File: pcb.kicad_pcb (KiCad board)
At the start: 2 copper layers, 47 x 68 mm, 52 parts, among them J1 SWD, J10 Conn_02x04_Counter_Clockwise, J2 PWR, J3 MPU6050, J4 ENC1, J5 ENC2, J6 ENC3, J7 USB_C_Receptacle_USB2.0_14P, J8 MA, J9 MB, SW1 SW_Push, U1 STM32F401RBTx, U2 LD1117S50TR_SOT223, U3 TB6612FNG, U4 USBLC6-2SC6, U5 LD1117S33TR_SOT223

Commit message: Initial routing
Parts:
- moved J1 14.0 mm to (78.5, 140.2)
- moved S2 12.0 mm to (96.6, 95.8), turned to 90 degrees
- moved J3 10.9 mm to (53.2, 141.1), turned to 180 degrees
- moved J4 7.68 mm to (61.0, 85.0)
- moved J2 6.25 mm to (88.0, 85.0)
- moved J5 6.25 mm to (74.5, 85.0)
- moved R10 4.22 mm to (72.5, 124.0)
- moved C5 2.01 mm to (58.4, 112.3)
- moved C18 2.00 mm to (60.4, 112.3)
- moved C17 0.22 mm to (72.5, 120.0)
- moved D4 0.22 mm to (72.5, 122.0)
- moved C2 0.20 mm to (74.4, 118.0)
- moved J10 0.19 mm to (85.0, 140.2)
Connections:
- U1 pad 37: /ENC_A -> /ENC_B
- U1 pad 38: /ENC_B -> /ENC_A
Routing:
- net /ESD_D-: track 0.00 -> 10.3 mm
- net /ESD_D+: track 0.00 -> 10.3 mm
- net /RSTN: track 0.00 -> 9.07 mm
- net Net-(R8-Pad1): track 0.00 -> 8.82 mm
- net /USER_LED: track 0.00 -> 8.00 mm
- net GND: track 0.00 -> 7.06 mm, vias 0 -> 28
- net +3.3V: track 0.00 -> 6.38 mm
- net Net-(U1-BOOT0): track 0.00 -> 5.38 mm
- net /USB_D-: track 0.00 -> 5.37 mm
- net /USB_D+: track 0.00 -> 5.14 mm
- net Net-(J10-Pin_3): track 0.00 -> 3.17 mm
- net Net-(U1-VCAP1): track 0.00 -> 2.95 mm
- net Net-(D4-A): track 0.00 -> 2.77 mm
- net /CONN_D-: track 0.00 -> 2.18 mm
- net /CONN_D+: track 0.00 -> 2.18 mm
- added copper zone on F.Cu, net +3.3V
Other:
- outline, holes or cut-outs redrawn

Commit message: First finished board
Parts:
- moved J1 53.7 mm to (53.4, 92.8), turned to 90 degrees
- moved J2 32.9 mm to (95.5, 117.0), turned to -90 degrees
- moved J6 23.4 mm to (84.8, 147.0), turned to 180 degrees
- moved J10 9.04 mm to (94.0, 141.6), turned to 180 degrees
- moved C10 8.50 mm to (97.2, 126.5)
- moved D2 8.50 mm to (92.2, 127.5)
- moved R9 6.86 mm to (91.2, 138.0), turned to -90 degrees
- moved R7 0.43 mm to (84.5, 109.8)
- moved R6 0.32 mm to (84.5, 107.5)
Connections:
- U1 pad 21: /M_A1 -> /M_A2
- U1 pad 22: /M_A2 -> /M_A1
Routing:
- net +3.3V: track 6.38 -> 170.7 mm, vias 0 -> 10
- net +BATT: track 0.00 -> 87.5 mm, vias 0 -> 3
- net +5V: track 0.00 -> 84.8 mm
- net /ENC_SCL: track 0.00 -> 51.6 mm, vias 0 -> 4
- net /ESP_RX: track 0.00 -> 44.9 mm, vias 0 -> 4
- net /ENC_A: track 0.00 -> 41.3 mm, vias 0 -> 2
- net /ESP_TX: track 0.00 -> 38.9 mm, vias 0 -> 4
- net /ENC_B: track 0.00 -> 38.7 mm, vias 0 -> 2
- net /ENC_SDA: track 0.00 -> 38.2 mm, vias 0 -> 2
- net /IMU_SCL: track 0.00 -> 36.9 mm, vias 0 -> 2
- net /IMU_SDA: track 0.00 -> 34.8 mm, vias 0 -> 2
- net /SWDIO: track 0.00 -> 30.0 mm, vias 0 -> 2
- net /LED_DATA: track 0.00 -> 27.1 mm, vias 0 -> 2
- net /IMU_INT: track 0.00 -> 26.4 mm, vias 0 -> 2
- net /PWM_B: track 0.00 -> 23.8 mm, vias 0 -> 2
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- added copper zone on F.Cu, net +5VP
- added copper zone on F.Cu, net Net-(J8-Pin_1)
- added copper zone on F.Cu, net Net-(J8-Pin_2)
- added copper zone on F.Cu, net Net-(J9-Pin_1)
- added copper zone on F.Cu, net Net-(J9-Pin_2)

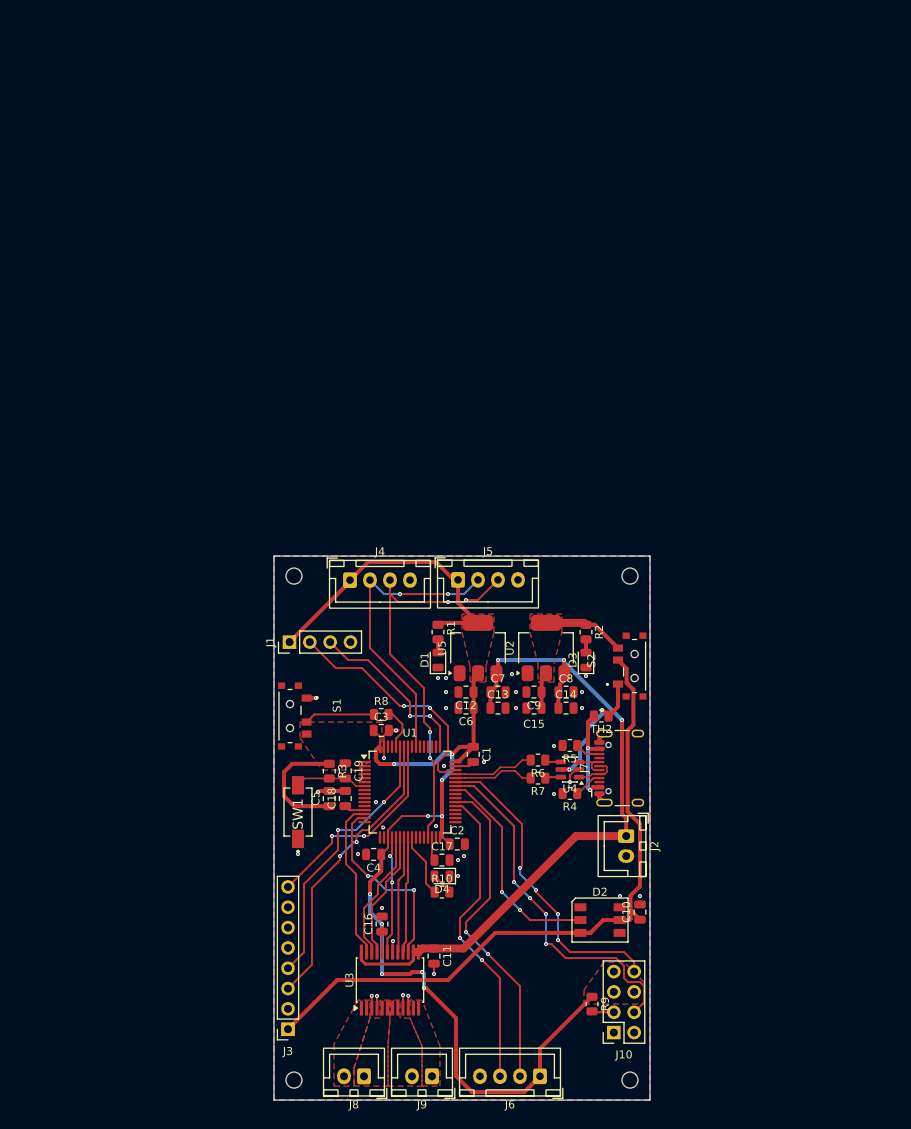
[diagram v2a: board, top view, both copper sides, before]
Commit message: Updated to given schematic
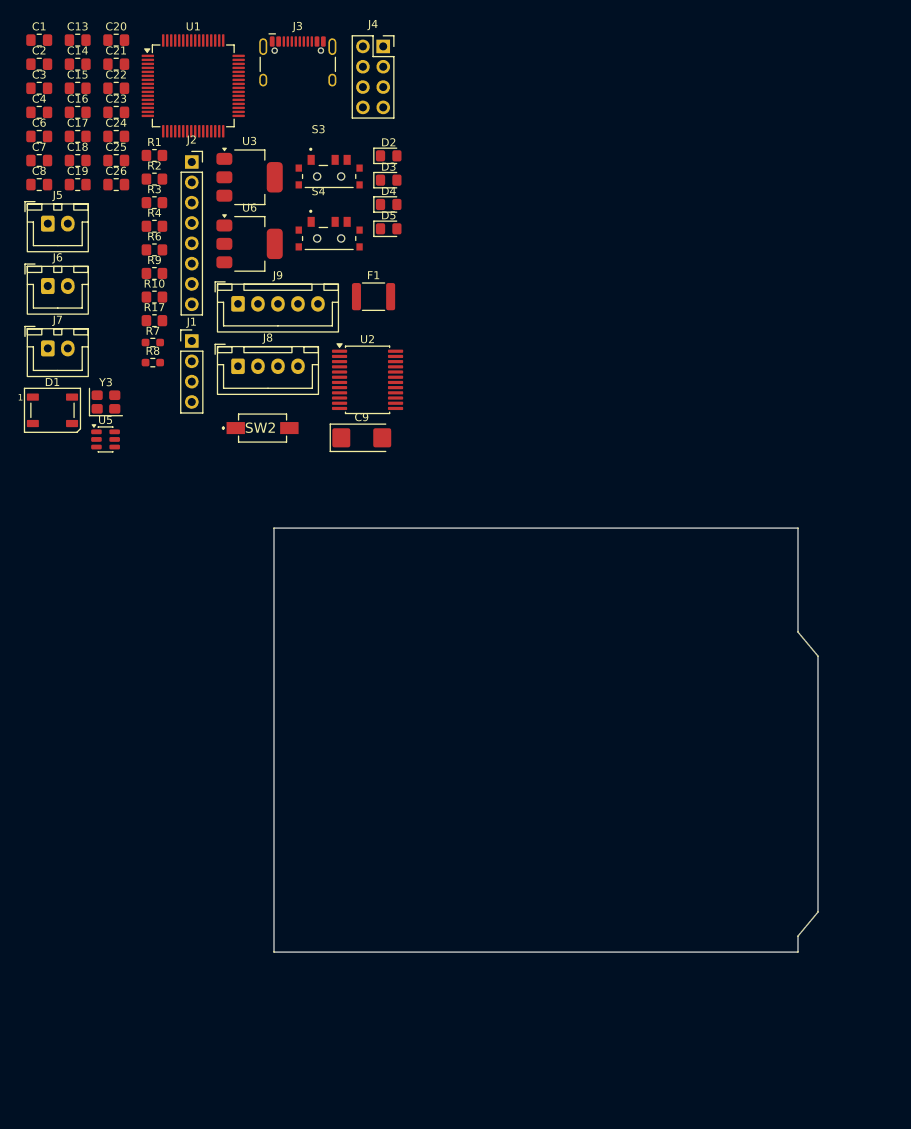
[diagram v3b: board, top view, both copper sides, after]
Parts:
- removed C10, C5: 10uF, Capacitor_SMD:C_0805_2012Metric
- removed C11: 22uF, Capacitor_SMD:C_0805_2012Metric
- removed C12: 100nF, Capacitor_SMD:C_0805_2012Metric
- removed J10: Conn_02x04_Counter_Clockwise, Connector_PinSocket_2.54mm:PinSocket_2x04_P2.54mm_Vertical
- removed R5: 5k1, Resistor_SMD:R_0805_2012Metric
- removed S1, S2: SLW-66527511-SMT-TR, SW_SLW-66527511-SMT-TR:SW_SLW-66527511-SMT-TR
- removed SW1: SW_Push, SW_uP_Reset:SW_uP_Reset
- removed TH2: Thermistor_PTC, Resistor_SMD:R_0805_2012Metric
- removed U4: USBLC6-2SC6, Package_TO_SOT_SMD:SOT-23-6
- added C20: 22p, Capacitor_SMD:C_0805_2012Metric_Pad1.18x1.45mm_HandSolder, F.Cu at (31.8, 17.5)
- added C21: 0.01uF, Capacitor_SMD:C_0805_2012Metric_Pad1.18x1.45mm_HandSolder, F.Cu at (31.8, 20.5)
- added C22: 0.1uF, Capacitor_SMD:C_0805_2012Metric_Pad1.18x1.45mm_HandSolder, F.Cu at (31.8, 23.5)
- added C23: 10uF, Capacitor_SMD:C_0805_2012Metric_Pad1.18x1.45mm_HandSolder, F.Cu at (31.8, 26.5)
- added C24: 0.1uF, Capacitor_SMD:C_0805_2012Metric_Pad1.18x1.45mm_HandSolder, F.Cu at (31.8, 29.5)
- added C25: 10uF, Capacitor_SMD:C_0805_2012Metric_Pad1.18x1.45mm_HandSolder, F.Cu at (31.8, 32.6)
- added C26: 0.1uF, Capacitor_SMD:C_0805_2012Metric_Pad1.18x1.45mm_HandSolder, F.Cu at (31.8, 35.6)
- added D5: 5V_LED, LED_SMD:LED_0805_2012Metric_Pad1.15x1.40mm_HandSolder, F.Cu at (65.8, 41.1)
- added F1: PTCSMD, Fuse:Fuse_1812_4532Metric, F.Cu at (63.9, 49.6)
- added R17: 10k, Resistor_SMD:R_0805_2012Metric_Pad1.20x1.40mm_HandSolder, F.Cu at (36.6, 52.6)
- added S3: REGULATOR_SWITCH, SW_SLW-66527511-SMT-TR:SW_SLW-66527511-SMT-TR, F.Cu at (58.4, 34.5)
- added S4: RST_SWITCH, SW_SLW-66527511-SMT-TR:SW_SLW-66527511-SMT-TR, F.Cu at (58.4, 42.3)
- added SW2: SW_uP_Reset, SW_uP_Reset:SW_uP_Reset, F.Cu at (50.1, 66.0)
- added U6: LD1117S33TR_SOT223, Package_TO_SOT_SMD:SOT-223-3_TabPin2, F.Cu at (48.4, 43.0)
- added Y3: 16MHz, Crystal:Crystal_SMD_Abracon_ABM8G-4Pin_3.2x2.5mm, F.Cu at (30.5, 62.7)
- C1, C13, C14, C2, C3, C4: value 100nF -> 0.1uF; footprint Capacitor_SMD:C_0805_2012Metric -> Capacitor_SMD:C_0805_2012Metric_Pad1.18x1.45mm_HandSolder
- C15, C16, C18: value 100nF -> 10uF; footprint Capacitor_SMD:C_0805_2012Metric -> Capacitor_SMD:C_0805_2012Metric_Pad1.18x1.45mm_HandSolder
- C17: value 2.2uF -> 0.1uF; footprint Capacitor_SMD:C_0805_2012Metric -> Capacitor_SMD:C_0805_2012Metric_Pad1.18x1.45mm_HandSolder
- C19: value 100nF -> 22p; footprint Capacitor_SMD:C_0805_2012Metric -> Capacitor_SMD:C_0805_2012Metric_Pad1.18x1.45mm_HandSolder
- C6, C8: value 10uF -> 0.1uF; footprint Capacitor_SMD:C_0805_2012Metric -> Capacitor_SMD:C_0805_2012Metric_Pad1.18x1.45mm_HandSolder
- C7: value 10uF -> 2.2uF; footprint Capacitor_SMD:C_0805_2012Metric -> Capacitor_SMD:C_0805_2012Metric_Pad1.18x1.45mm_HandSolder
- C9: footprint Capacitor_SMD:C_0805_2012Metric -> Capacitor_Tantalum_SMD:CP_EIA-6032-28_Kemet-C_HandSolder
- D1: value LED -> WS2812B; footprint LED_SMD:LED_0805_2012Metric -> LED_SMD:LED_WS2812B_PLCC4_5.0x5.0mm_P3.2mm
- D2: value WS2812 -> USB_LED; footprint LED_SMD:LED_WS2812_PLCC6_5.0x5.0mm_P1.6mm -> LED_SMD:LED_0805_2012Metric_Pad1.15x1.40mm_HandSolder
- D3: value LED -> 3V3_LED; footprint LED_SMD:LED_0805_2012Metric -> LED_SMD:LED_0805_2012Metric_Pad1.15x1.40mm_HandSolder
- D4: value LED -> USER_LED; footprint LED_SMD:LED_0805_2012Metric -> LED_SMD:LED_0805_2012Metric_Pad1.15x1.40mm_HandSolder
- J1: value SWD -> Conn_01x04
- J2: value PWR -> CONN_MPU6050; footprint Connector_JST:JST_XH_B2B-XH-A_1x02_P2.50mm_Vertical -> Connector_PinSocket_2.54mm:PinSocket_1x08_P2.54mm_Vertical
- J3: value MPU6050 -> USB_C_Receptacle_USB2.0_14P; footprint Connector_PinSocket_2.54mm:PinSocket_1x08_P2.54mm_Vertical -> Connector_USB:USB_C_Receptacle_HCTL_HC-TYPE-C-16P-01A
- J4: value ENC1 -> ESP_Conn; footprint Connector_JST:JST_XH_B4B-XH-A_1x04_P2.50mm_Vertical -> Connector_PinSocket_2.54mm:PinSocket_2x04_P2.54mm_Vertical
- J5: value ENC2 -> BATT_CONN; footprint Connector_JST:JST_XH_B4B-XH-A_1x04_P2.50mm_Vertical -> Connector_JST:JST_XH_B2B-XH-A_1x02_P2.50mm_Vertical
- J6: value ENC3 -> M1_CONN; footprint Connector_JST:JST_XH_B4B-XH-A_1x04_P2.50mm_Vertical -> Connector_JST:JST_XH_B2B-XH-A_1x02_P2.50mm_Vertical
- J7: value USB_C_Receptacle_USB2.0_14P -> M2_CONN; footprint Connector_USB:USB_C_Receptacle_HCTL_HC-TYPE-C-16P-01A -> Connector_JST:JST_XH_B2B-XH-A_1x02_P2.50mm_Vertical
- J8: value MA -> ENCODER_CONN; footprint Connector_JST:JST_XH_B2B-XH-A_1x02_P2.50mm_Vertical -> Connector_JST:JST_XH_B4B-XH-A_1x04_P2.50mm_Vertical
- J9: value MB -> MT6701_CONN; footprint Connector_JST:JST_XH_B2B-XH-A_1x02_P2.50mm_Vertical -> Connector_JST:JST_XH_B5B-XH-A_1x05_P2.50mm_Vertical
- R1, R10: footprint Resistor_SMD:R_0805_2012Metric -> Resistor_SMD:R_0805_2012Metric_Pad1.20x1.40mm_HandSolder
- R2: value 1k -> 10k; footprint Resistor_SMD:R_0805_2012Metric -> Resistor_SMD:R_0805_2012Metric_Pad1.20x1.40mm_HandSolder
- R3: value 1k -> 22R; footprint Resistor_SMD:R_0805_2012Metric -> Resistor_SMD:R_0805_2012Metric_Pad1.20x1.40mm_HandSolder
- R4: value 5k1 -> 22R; footprint Resistor_SMD:R_0805_2012Metric -> Resistor_SMD:R_0805_2012Metric_Pad1.20x1.40mm_HandSolder
- R6: value 22 -> 1k; footprint Resistor_SMD:R_0805_2012Metric -> Resistor_SMD:R_0805_2012Metric_Pad1.20x1.40mm_HandSolder
- R7: value 22 -> 5.1k; footprint Resistor_SMD:R_0805_2012Metric -> Resistor_SMD:R_0603_1608Metric_Pad0.98x0.95mm_HandSolder
- R8: value 10k -> 5.1k; footprint Resistor_SMD:R_0805_2012Metric -> Resistor_SMD:R_0603_1608Metric_Pad0.98x0.95mm_HandSolder
- R9: value 10k -> 1k; footprint Resistor_SMD:R_0805_2012Metric -> Resistor_SMD:R_0805_2012Metric_Pad1.20x1.40mm_HandSolder
- U2: value LD1117S50TR_SOT223 -> TB6612FNG; footprint Package_TO_SOT_SMD:SOT-223-3_TabPin2 -> Package_SO:SSOP-24_5.3x8.2mm_P0.65mm
- U3: value TB6612FNG -> LD1117S50TR_SOT223; footprint Package_SO:SSOP-24_5.3x8.2mm_P0.65mm -> Package_TO_SOT_SMD:SOT-223-3_TabPin2
- U5: value LD1117S33TR_SOT223 -> USBLC6-2SC6; footprint Package_TO_SOT_SMD:SOT-223-3_TabPin2 -> Package_TO_SOT_SMD:SOT-23-6
- moved J3 119.7 mm to (54.5, 21.4), turned to 0 degrees
- moved J6 116.4 mm to (23.2, 48.2), turned to 0 degrees
- moved C2 110.6 mm to (22.2, 20.5)
- moved C16 108.4 mm to (27.0, 26.5), turned to 0 degrees
- moved R9 106.5 mm to (36.6, 46.7), turned to 0 degrees
- moved C1 104.5 mm to (22.2, 17.5), turned to 0 degrees
- moved U3 101.9 mm to (48.4, 34.6), turned to 0 degrees
- moved C4 101.7 mm to (22.2, 26.5), turned to 0 degrees
- moved C17 101.3 mm to (27.0, 29.5)
- moved C14 101.0 mm to (27.0, 20.5)
- moved J2 100.2 mm to (41.2, 32.7), turned to 0 degrees
- moved J9 99.6 mm to (47.0, 50.5), turned to 0 degrees
- moved D2 99.1 mm to (65.8, 32.0)
- moved C13 98.6 mm to (27.0, 17.5)
- moved C15 96.2 mm to (27.0, 23.5), turned to 0 degrees
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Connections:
- C13 pad 1: +BATT -> +5V
- C14 pad 1: +BATT -> +3.3V
- C15 pad 1: +5VP -> +5V
- C17 pad 1: Net-(U1-VCAP1) -> VM
- C18 pad 1: Net-(U1-VREF+) -> VM
- C19 pad 1: +3.3V -> GND
- C19 pad 2: /RSTN -> /OSCIN
- C6 pad 1: +3.3V -> VM
- C7 pad 1: +BATT -> Net-(U1-VCAP1)
- C8 pad 1: +BATT -> +3.3V
- C9 pad 1: +5VP -> VM
- D1 pad 1: GND -> +5V
- D1 pad 2: Net-(D1-A) -> unconnected-(D1-DOUT-Pad2)
- D2 pad 1: unconnected-(D2-DOUT-Pad1) -> GND
- D2 pad 2: /LED_DATA -> Net-(D2-A)
- J1 pad 2: /SWDIO -> /SWCLK
- J1 pad 3: /SWCLK -> GND
- J1 pad 4: GND -> /SWDIO
- J2 pad 1: +BATT -> +5V
- J4 pad 1: +3.3V -> GND
- J4 pad 2: /ENC_SDA -> /ESP_TX
- J4 pad 3: /ENC_SCL -> unconnected-(J4-Pin_3-Pad3)
- J4 pad 4: GND -> +3.3V
- J5 pad 1: +3.3V -> VM
- J5 pad 2: /ENC_SDA -> GND
- J6 pad 1: +3.3V -> /MD_AO1
- J6 pad 2: /ENC_A -> /MD_AO2
- J8 pad 1: Net-(J8-Pin_1) -> +3.3V
- J8 pad 2: Net-(J8-Pin_2) -> /ENC_A
- J9 pad 1: Net-(J9-Pin_1) -> +3.3V
- J9 pad 2: Net-(J9-Pin_2) -> GND
- R1 pad 1: +3.3V -> Net-(D2-A)
- R1 pad 2: Net-(D1-A) -> Vusb
- R10 pad 1: /USER_LED -> Net-(D5-A)
- R10 pad 2: Net-(D4-A) -> 5V_REG
- R2 pad 1: +5VP -> Net-(R2-~-Pad1)
- R2 pad 2: Net-(D3-A) -> /BOOT0
- R3 pad 1: +3.3V -> /CONN_D-
- R3 pad 2: /RSTN -> /ESD_D-
- R4 pad 1: Net-(J7-CC1) -> /CONN_D+
- R4 pad 2: GND -> /ESD_D+
- R6 pad 1: /CONN_D+ -> Net-(D3-A)
- R6 pad 2: /ESD_D+ -> +3.3V
- R7 pad 1: /CONN_D- -> GND
- R7 pad 2: /ESD_D- -> Net-(J3-CC1)
- R8 pad 1: Net-(R8-Pad1) -> Net-(J3-CC2)
- R8 pad 2: Net-(U1-BOOT0) -> GND
- R9 pad 1: +3.3V -> Net-(D4-A)
- R9 pad 2: Net-(J10-Pin_3) -> /USER_LED
- U1 pad 13: Net-(U1-VREF+) -> +3.3V
- U1 pad 14: /PWM_A -> /WS_DIN
- U1 pad 15: /PWM_B -> /MD_PWMA
- U1 pad 16: unconnected-(U1-PA2-Pad16) -> /MD_AIN2
- U1 pad 17: unconnected-(U1-PA3-Pad17) -> /MD_AIN1
- U1 pad 2: unconnected-(U1-PC13-Pad2) -> /IMU_INT
- U1 pad 20: /M_STBY -> /MD_STBY
- U1 pad 21: /M_A2 -> /MD_PWMB
- U1 pad 22: /M_A1 -> /MD_BIN1
- U1 pad 23: /M_B1 -> /MD_BIN2
- U1 pad 24: /M_B2 -> unconnected-(U1-PC4-Pad24)
- U1 pad 25: /USER_LED -> unconnected-(U1-PC5-Pad25)
- U1 pad 27: unconnected-(U1-PB1-Pad27) -> /USER_LED
- U1 pad 28: unconnected-(U1-PB2-Pad28) -> GND
- U1 pad 29: /ENC_SCL -> unconnected-(U1-PB10-Pad29)
- U1 pad 37: /ENC_B -> /MT_PWM
- U1 pad 38: /ENC_A -> unconnected-(U1-PC7-Pad38)
- U1 pad 40: unconnected-(U1-PC9-Pad40) -> /MT_SDA
- U1 pad 41: /LED_DATA -> /MT_SCL
- U1 pad 5: unconnected-(U1-PH0-Pad5) -> /OSCIN
- U1 pad 55: /ENC_SDA -> unconnected-(U1-PB3-Pad55)
- U1 pad 57: /IMU_INT -> unconnected-(U1-PB5-Pad57)
- U1 pad 58: /IMU_SCL -> /ENC_B
- U1 pad 59: /IMU_SDA -> /ENC_A
- U1 pad 6: unconnected-(U1-PH1-Pad6) -> /OSCOUT
- U1 pad 60: Net-(U1-BOOT0) -> /BOOT0
- U1 pad 61: unconnected-(U1-PB8-Pad61) -> /IMU_SCL
- U1 pad 62: unconnected-(U1-PB9-Pad62) -> /IMU_SDA
- U1 pad 7: /RSTN -> /RESET
- U2 pad 1: GND -> /MD_AO1
- U2 pad 2: +5VP -> /MD_AO1
- U2 pad 3: +BATT -> GND
- U3 pad 1: Net-(J8-Pin_2) -> GND
- U3 pad 2: Net-(J8-Pin_2) -> 5V_REG
- U3 pad 3: GND -> VM
- U5 pad 1: GND -> /USB_D-
- U5 pad 2: +3.3V -> GND
- U5 pad 3: +BATT -> /USB_D+
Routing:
- net +3.3V: track 170.7 -> 0.00 mm, vias 10 -> 0
- net +BATT: track 87.5 -> 0.00 mm, vias 3 -> 0
- net +5V: track 84.8 -> 0.00 mm
- net /ENC_SCL: track 51.6 -> 0.00 mm, vias 4 -> 0
- net /ESP_RX: track 44.9 -> 0.00 mm, vias 4 -> 0
- net /ENC_A: track 41.3 -> 0.00 mm, vias 2 -> 0
- net /ESP_TX: track 38.9 -> 0.00 mm, vias 4 -> 0
- net /ENC_B: track 38.7 -> 0.00 mm, vias 2 -> 0
- net /ENC_SDA: track 38.2 -> 0.00 mm, vias 2 -> 0
- net /IMU_SCL: track 36.9 -> 0.00 mm, vias 2 -> 0
- net /IMU_SDA: track 34.8 -> 0.00 mm, vias 2 -> 0
- net /SWDIO: track 30.0 -> 0.00 mm, vias 2 -> 0
- net /LED_DATA: track 27.1 -> 0.00 mm, vias 2 -> 0
- net /IMU_INT: track 26.4 -> 0.00 mm, vias 2 -> 0
- net GND: track 26.0 -> 0.00 mm, vias 36 -> 0
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- removed copper zone on F.Cu, net +3.3V
- removed copper zone on F.Cu, net +5VP
- removed copper zone on B.Cu, net GND
- removed copper zone on F.Cu, net GND
- removed copper zone on F.Cu, net Net-(J8-Pin_1)
- removed copper zone on F.Cu, net Net-(J8-Pin_2)
- removed copper zone on F.Cu, net Net-(J9-Pin_1)
- removed copper zone on F.Cu, net Net-(J9-Pin_2)
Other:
- board size 47 x 68 mm -> 68 x 53 mm

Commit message: Initial uno layout
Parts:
- added H1: MountingHole, MountingHole:MountingHole_3.2mm_M3, F.Cu at (74.5, 94.5)
- added H2: MountingHole, MountingHole:MountingHole_3.2mm_M3, F.Cu at (124.0, 137.0)
- added H3: MountingHole, MountingHole:MountingHole_3.2mm_M3, F.Cu at (124.0, 109.0)
- added H4: MountingHole, MountingHole:MountingHole_3.2mm_M3, F.Cu at (74.5, 140.5)
- moved C1 129.5 mm to (105.0, 117.0), turned to 180 degrees
- moved C2 120.1 mm to (108.0, 104.5), turned to -90 degrees
- moved C7 119.7 mm to (105.0, 119.0)
- moved C26 118.2 mm to (117.0, 117.5), turned to 180 degrees
- moved C6 117.6 mm to (85.8, 128.5), turned to -90 degrees
- moved C13 116.9 mm to (71.8, 125.5), turned to 90 degrees
- moved J9 114.2 mm to (116.0, 141.5), turned to 180 degrees
- moved J6 113.5 mm to (88.2, 141.3), turned to 180 degrees
- moved C22 113.5 mm to (71.8, 129.7), turned to 90 degrees
- moved C17 113.2 mm to (71.8, 133.5), turned to 90 degrees
- moved J7 112.6 mm to (96.8, 141.3), turned to 180 degrees
- moved C8 112.3 mm to (91.0, 124.2)
- moved C14 110.7 mm to (71.8, 121.7), turned to 90 degrees
- moved C15 110.6 mm to (69.8, 125.5), turned to 90 degrees
- moved C23 109.9 mm to (69.8, 129.7), turned to 90 degrees
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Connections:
- S3 pad 1: 5V_REG -> Vusb
- S3 pad 3: Vusb -> 5V_REG

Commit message: Finished pcb
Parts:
- added G***: LOGO, Logo:Logo_D, F.Cu at (111.0, 124.7)
- added G***: LOGO, Logo:Logo_U, F.Cu at (111.0, 124.7)
- moved C26 17.9 mm to (102.5, 128.0)
- moved D1 17.9 mm to (101.0, 124.0)
- moved J1 7.83 mm to (115.0, 134.7)
- moved J9 5.76 mm to (110.2, 141.3)
- moved C6 3.20 mm to (83.2, 126.5), turned to 90 degrees
- moved C8 2.50 mm to (88.5, 124.2)
- moved C9 2.50 mm to (95.2, 131.0)
- moved J6 2.50 mm to (85.8, 141.3)
- moved J7 2.50 mm to (94.2, 141.3)
- moved U2 2.50 mm to (88.8, 131.0)
- moved R4 2.46 mm to (74.5, 104.8)
- moved R2 2.02 mm to (106.5, 97.0)
- moved R3 2.02 mm to (74.5, 106.8)
- moved S3 0.50 mm to (61.5, 123.5)
- moved S4 0.50 mm to (108.0, 93.0)
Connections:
- J2 pad 1: +5V -> +3.3V
- J6 pad 1: /MD_AO1 -> /MD_AO2
- J6 pad 2: /MD_AO2 -> /MD_AO1
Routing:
- net +3.3V: track 0.00 -> 180.8 mm, vias 0 -> 21
- net GND: track 0.00 -> 92.1 mm, vias 0 -> 37
- net +5V: track 0.00 -> 73.4 mm, vias 0 -> 2
- net /SWDIO: track 0.00 -> 48.1 mm, vias 0 -> 2
- net /SWCLK: track 0.00 -> 46.3 mm, vias 0 -> 4
- net /MT_SCL: track 0.00 -> 45.1 mm, vias 0 -> 2
- net /ENC_A: track 0.00 -> 39.8 mm, vias 0 -> 2
- net /ENC_B: track 0.00 -> 39.3 mm, vias 0 -> 2
- net /RESET: track 0.00 -> 39.1 mm, vias 0 -> 4
- net /MT_SDA: track 0.00 -> 38.7 mm, vias 0 -> 2
- net /USER_LED: track 0.00 -> 34.0 mm, vias 0 -> 2
- net /ESD_D-: track 0.00 -> 33.7 mm
- net /ESD_D+: track 0.00 -> 33.7 mm
- net /MT_PWM: track 0.00 -> 33.4 mm
- net 5V_REG: track 0.00 -> 32.1 mm
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- added copper zone on F.Cu, net +3.3V
- added copper zone on F.Cu, net /MD_AO1
- added copper zone on F.Cu, net /MD_AO2
- added copper zone on F.Cu, net /MD_BO1
- added copper zone on F.Cu, net /MD_BO2
- added copper zone on F.Cu, net 5V_REG
- added copper zone on B.Cu, net GND
- added copper zone on F.Cu, net GND
- added copper zone on F.Cu, net VM
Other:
- board text added: "3V"
- board text added: "3V3 A B GND"
- board text added: "3V3 SWCLK GND SWDIO"
- board text added: "5V"
- board text added: "BATT"
- board text added: "BOOT"
- board text added: "DFU"
- board text added: "ENCODER"
- board text added: "ESP"
- board text added: "INT - NC - SDA SCL GND 3V3"
- board text added: "MOTOR A"
- board text added: "MOTOR B"
- board text added: "MPU6050"
- board text added: "MT6701"
- board text added: "Matthew Murray"
- board text added: "Motor Driver"
- board text added: "RESET"
- board text added: "Regulators"
- board text added: "SDA SCL PWM GND 3V3"
- board text added: "USB"
- board text added: "VREG"
- board text added: "VUSB"
- board text added: "VUSB 5V 3V3 USER"

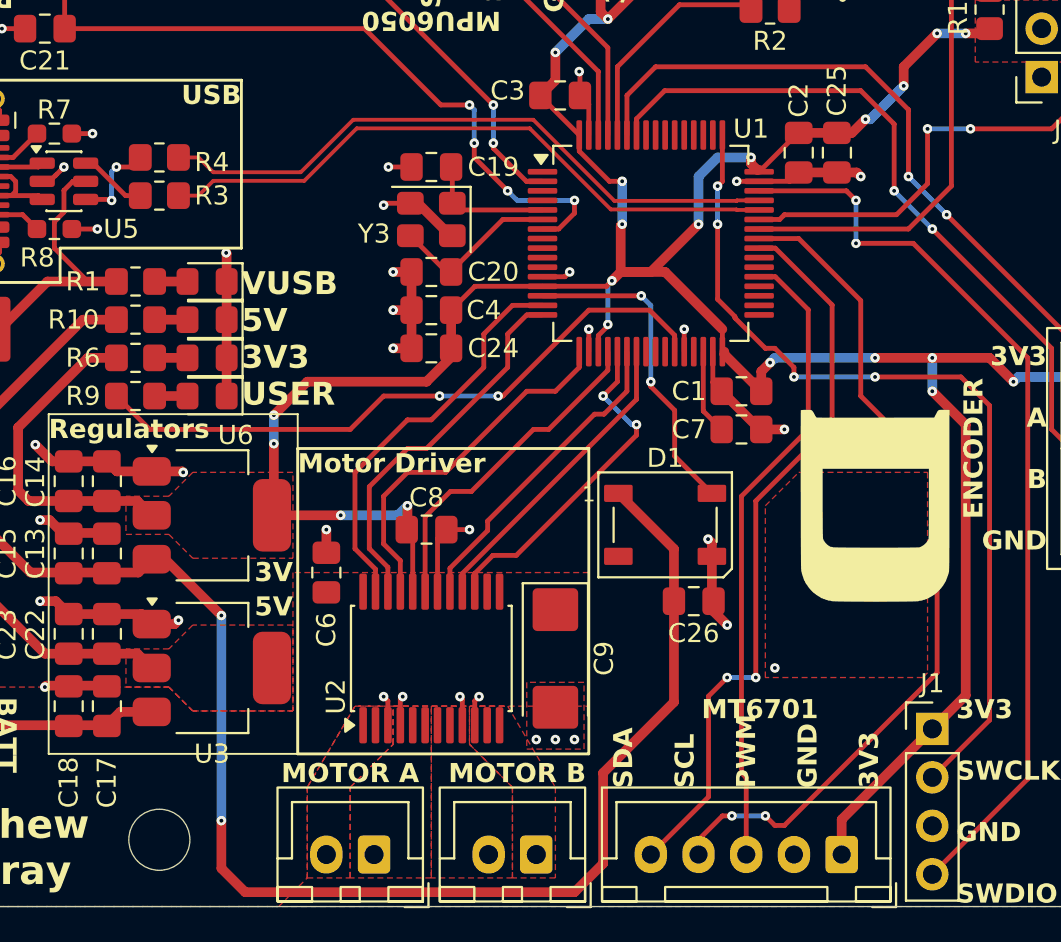
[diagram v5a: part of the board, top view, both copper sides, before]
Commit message: Added pullups
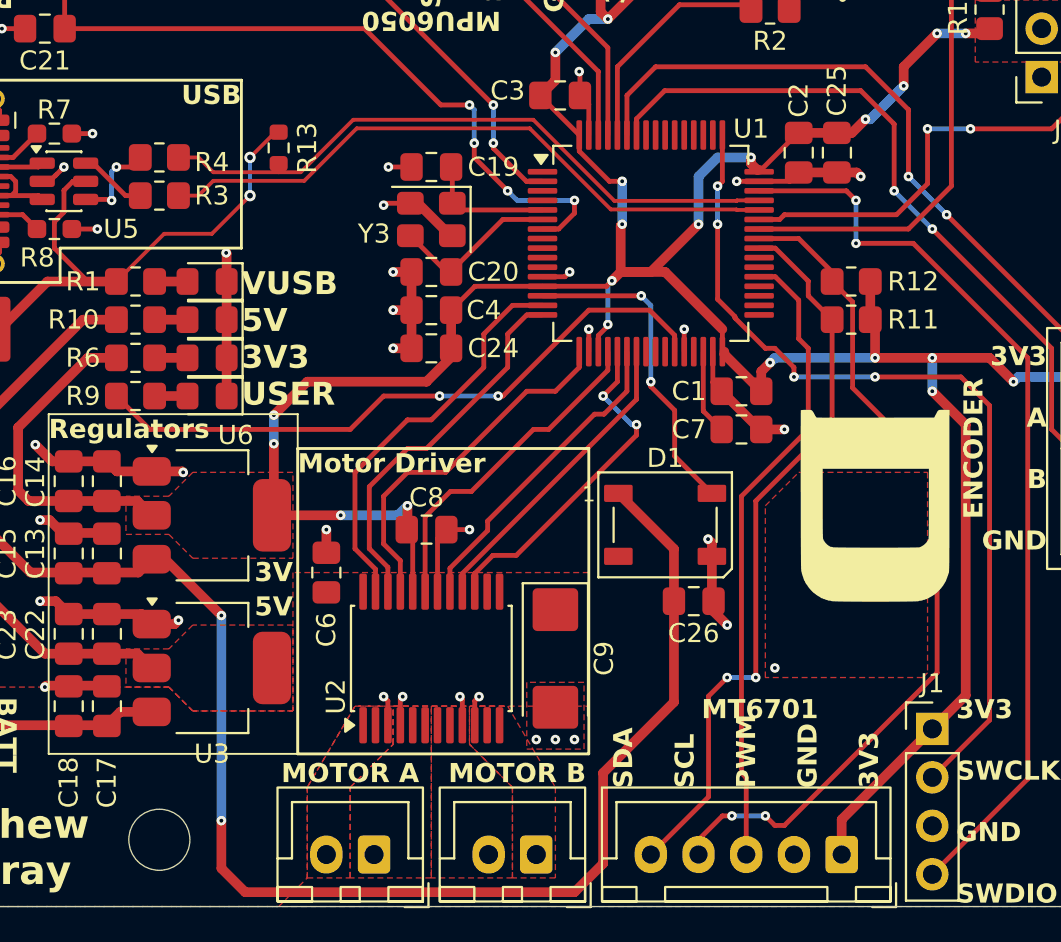
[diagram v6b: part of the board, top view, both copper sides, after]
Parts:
- added R11: 1k, Resistor_SMD:R_0805_2012Metric_Pad1.20x1.40mm_HandSolder, F.Cu at (110.8, 113.2)
- added R12: 1k, Resistor_SMD:R_0805_2012Metric_Pad1.20x1.40mm_HandSolder, F.Cu at (110.8, 111.2)
- added R13: 5.1k, Resistor_SMD:R_0603_1608Metric, F.Cu at (80.8, 104.2)
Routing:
- net Vusb: track 24.4 -> 37.3 mm, vias 0 -> 2
- net +3.3V: track 180.8 -> 184.9 mm
